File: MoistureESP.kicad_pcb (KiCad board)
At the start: 2 copper layers, 106 parts, among them J1 Conn_01x02_Pin, J2 Conn_MoisturePCB, J3 Conn_DS18B20, J4 Conn_01x06_Pin, J5 Conn_01x03_Pin, J7 USB4110-GF-A, Q1 SSM6K513NU-LF, Q10 SI7137DP-T1-GE3, Q2 SSM6K513NU-LF, Q3 2N7002W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

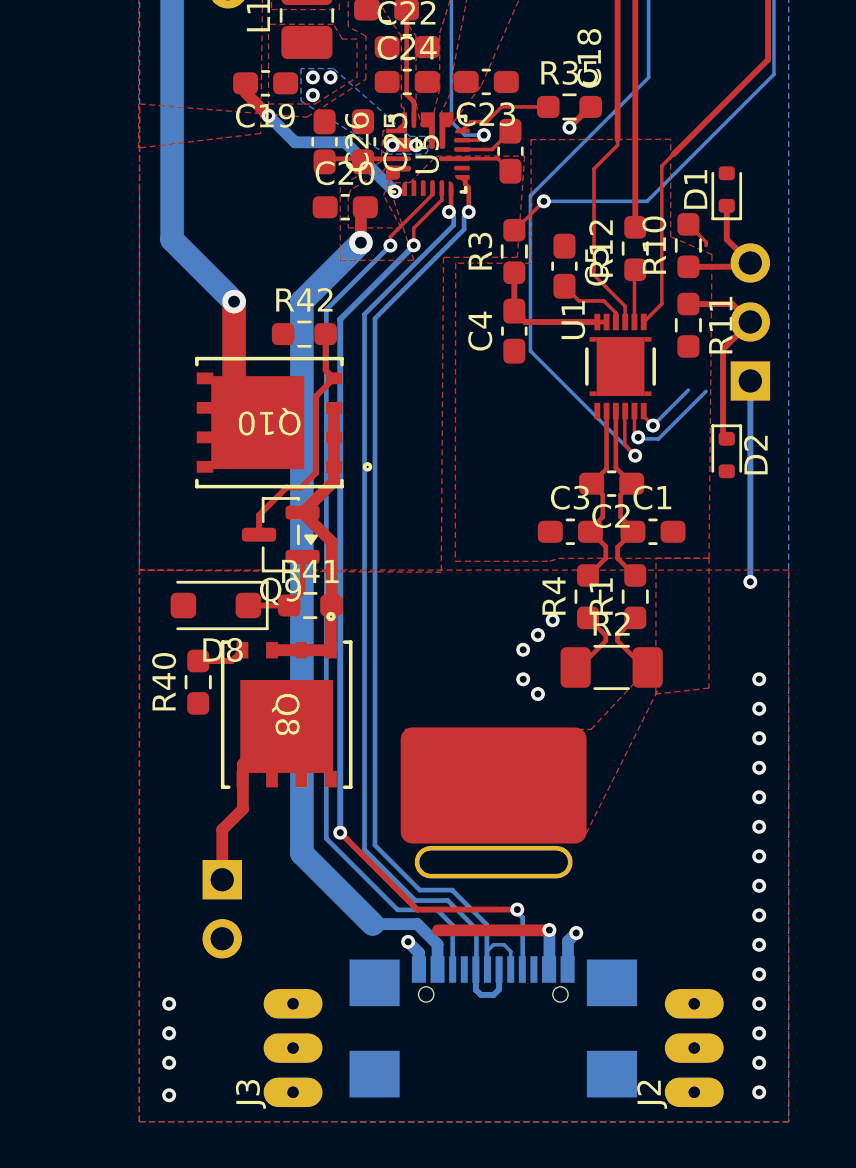
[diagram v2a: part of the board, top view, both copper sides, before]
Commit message: Change CGND connection to shunt resistor, change zone hierarchy.
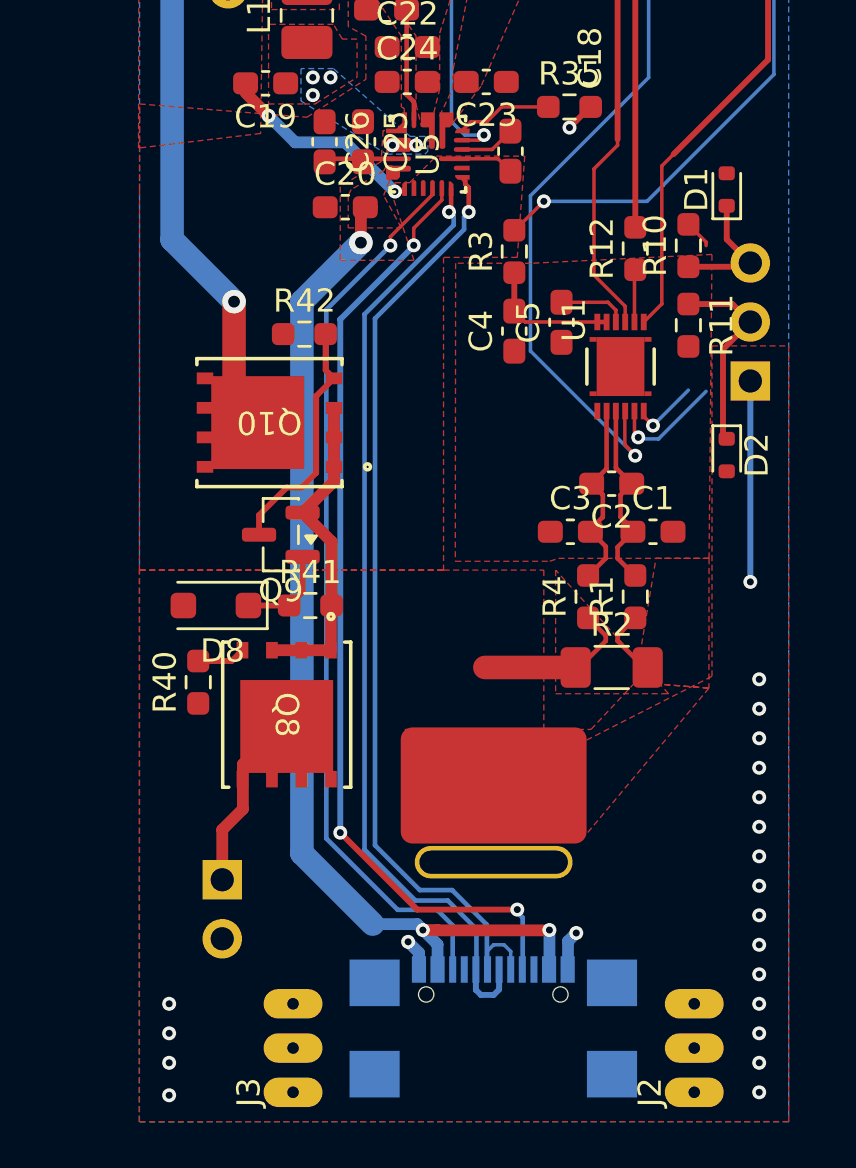
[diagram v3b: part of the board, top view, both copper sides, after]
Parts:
- moved C5 2.42 mm to (53.7, 118.0), turned to 90 degrees
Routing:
- net GNDPWR: track 15.7 -> 19.6 mm
- net VBUS: track 43.9 -> 44.6 mm, vias 2 -> 3
- net (no net): vias 24 -> 19
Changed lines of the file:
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@@
 	(footprint "Capacitor_SMD:C_0603_1608Metric_Pad1.08x0.95mm_HandSolder"
 		(layer "F.Cu")
-		(at 53.848 115.57 -90)
+		(at 53.721 117.983 90)
 		(descr "Capacitor SMD 0603 (1608 Metric), square (rectangular) end terminal, IPC-7351 nominal with elongated pad for handsoldering. (Body size source: IPC-SM-782 page 76, https://www.pcb-3d.com/wordpress/wp-content/uploads/ipc-sm-782a_amendment_1_and_2.pdf)")
 		(tags "capacitor handsolder")
@@
 		(duplicate_pad_numbers_are_jumpers no)
 		(fp_line
-			(start -0.146267 0.51)
-			(end 0.146267 0.51)
+			(start -0.146267 -0.51)
+			(end 0.146267 -0.51)
 			(stroke
 				(width 0.12)
@@
 		)
 		(fp_line
-			(start -0.146267 -0.51)
-			(end 0.146267 -0.51)
+			(start -0.146267 0.51)
+			(end 0.146267 0.51)
 			(stroke
 				(width 0.12)
@@
 		)
 		(pad "1" smd roundrect
-			(at -0.8625 0 270)
+			(at -0.8625 0 90)
 			(size 1.075 0.95)
 			(layers "F.Cu" "F.Mask" "F.Paste")
@@
 		)
 		(pad "2" smd roundrect
-			(at 0.8625 0 270)
+			(at 0.8625 0 90)
 			(size 1.075 0.95)
 			(layers "F.Cu" "F.Mask" "F.Paste")
@@
 	)
 	(via
-		(at 52.705 131.445)
-		(size 0.6)
-		(drill 0.3)
-		(layers "F.Cu" "B.Cu")
-		(net "")
-	)
-	(via
 		(at 62.23 143.51)
 		(size 0.6)
@@
 	)
 	(via
-		(at 53.34 130.81)
-		(size 0.6)
-		(drill 0.3)
-		(layers "F.Cu" "B.Cu")
-		(net "")
-	)
-	(via
-		(at 52.705 133.985)
-		(size 0.6)
-		(drill 0.3)
-		(layers "F.Cu" "B.Cu")
-		(net "")
-	)
-	(via
 		(at 36.83 148.59)
 		(size 0.6)
@@
 	)
 	(via
-		(at 52.07 132.08)
-		(size 0.6)
-		(drill 0.3)
-		(layers "F.Cu" "B.Cu")
-		(net "")
-	)
-	(via
 		(at 62.23 146.05)
 		(size 0.6)
@@
 	)
 	(via
-		(at 52.07 133.35)
-		(size 0.6)
-		(drill 0.3)
-		(layers "F.Cu" "B.Cu")
-		(net "")
-	)
-	(via
 		(at 62.23 148.59)
 		(size 0.6)
@@
 	)
 	(segment
+		(start 54.33 132.842)
+		(end 50.419 132.842)
+		(width 1.016)
+		(layer "F.Cu")
+		(net "GNDPWR")
+	)
+	(segment
 		(start 51.3435 107.636)
 		(end 51.3435 107.622)
@@
 	)
 	(segment
-		(start 54.4809 117.0654)
-		(end 53.848 116.4325)
-		(width 0.1524)
-		(layer "F.Cu")
-		(net "Net-(U1-PBI)")
-	)
-	(segment
-		(start 55.543501 117.0654)
-		(end 54.4809 117.0654)
+		(start 55.7192 117.1205)
+		(end 53.721 117.1205)
 		(width 0.1524)
 		(layer "F.Cu")
@@
 	(segment
 		(start 56.061 117.9703)
-		(end 56.061 117.582899)
+		(end 56.061 117.4623)
 		(width 0.1524)
 		(layer "F.Cu")
@@
 	)
 	(segment
-		(start 56.061 117.582899)
-		(end 55.543501 117.0654)
+		(start 56.061 117.4623)
+		(end 55.7192 117.1205)
 		(width 0.1524)
 		(layer "F.Cu")
@@
 	(segment
 		(start 52.1578 117.9703)
-		(end 51.689 117.5015)
-		(width 0.254)
+		(end 55.260999 117.9703)
+		(width 0.1524)
 		(layer "F.Cu")
 		(net "Net-(U1-VC1)")
@@
 	)
 	(segment
-		(start 55.661001 117.9703)
-		(end 55.661001 117.764001)
+		(start 51.689 117.5015)
+		(end 52.1578 117.9703)
 		(width 0.1524)
 		(layer "F.Cu")
@@
 	)
 	(segment
-		(start 55.260999 117.9703)
-		(end 52.1578 117.9703)
-		(width 0.254)
+		(start 55.661001 117.9703)
+		(end 55.661001 117.764001)
+		(width 0.1524)
 		(layer "F.Cu")
 		(net "Net-(U1-VC1)")
@@
 	)
 	(segment
+		(start 46.5105 110.144001)
+		(end 47.113501 110.144001)
+		(width 0.2)
+		(layer "F.Cu")
+		(net "Net-(U5-LX)")
+	)
+	(via
+		(at 43.0145 108.204)
+		(size 0.6)
+		(drill 0.3)
+		(layers "F.Cu" "B.Cu")
+		(free yes)
+		(net "Net-(U5-LX)")
+	)
+	(via
+		(at 43.7765 107.442)
+		(size 0.6)
+		(drill 0.3)
+		(layers "F.Cu" "B.Cu")
+		(free yes)
+		(net "Net-(U5-LX)")
+	)
+	(via
+		(at 46.4435 110.363)
+		(size 0.6)
+		(drill 0.3)
+		(layers "F.Cu" "B.Cu")
+		(net "Net-(U5-LX)")
+	)
+	(via
+		(at 43.0145 107.442)
+		(size 0.6)
+		(drill 0.3)
+		(layers "F.Cu" "B.Cu")
+		(free yes)
+		(net "Net-(U5-LX)")
+	)
+	(via
+		(at 47.4595 110.363)
+		(size 0.6)
+		(drill 0.3)
+		(layers "F.Cu" "B.Cu")
+		(net "Net-(U5-LX)")
+	)
+	(segment
 		(start 36.365999 92.0175)
 		(end 36.806 92.457501)
@@
 	(segment
 		(start 48.4 144.158)
+		(end 48.387 144.145)
+		(width 0.508)
+		(layer "F.Cu")
+		(net "VBUS")
+	)
+	(segment
+		(start 48.4 144.158)
 		(end 53.187 144.158)
 		(width 0.508)
@@
 	)
 	(segment
+		(start 48.387 144.145)
+		(end 47.752 144.145)
+		(width 0.508)
+		(layer "F.Cu")
+		(net "VBUS")
+	)
+	(segment
 		(start 45.085 114.554)
 		(end 45.085 113.219)
@@
 		(net "VBUS")
 	)
+	(via
+		(at 47.752 144.145)
+		(size 0.6)
+		(drill 0.3)
+		(layers "F.Cu" "B.Cu")
+		(net "VBUS")
+	)
 	(segment
 		(start 42.545 140.843)
@@
 		(net "Net-(U5-IFAST)")
 	)
-	(segment
-		(start 46.5105 110.144001)
-		(end 47.113501 110.144001)
-		(width 0.2)
-		(layer "F.Cu")
-		(net "Net-(U5-LX)")
-	)
-	(via
-		(at 43.0145 108.204)
-		(size 0.6)
-		(drill 0.3)
-		(layers "F.Cu" "B.Cu")
-		(free yes)
-		(net "Net-(U5-LX)")
-	)
-	(via
-		(at 43.7765 107.442)
-		(size 0.6)
-		(drill 0.3)
-		(layers "F.Cu" "B.Cu")
-		(free yes)
-		(net "Net-(U5-LX)")
-	)
-	(via
-		(at 46.4435 110.363)
-		(size 0.6)
-		(drill 0.3)
-		(layers "F.Cu" "B.Cu")
-		(net "Net-(U5-LX)")
-	)
-	(via
-		(at 43.0145 107.442)
-		(size 0.6)
-		(drill 0.3)
-		(layers "F.Cu" "B.Cu")
-		(free yes)
-		(net "Net-(U5-LX)")
-	)
-	(via
-		(at 47.4595 110.363)
-		(size 0.6)
-		(drill 0.3)
-		(layers "F.Cu" "B.Cu")
-		(net "Net-(U5-LX)")
-	)
 	(zone
 		(net "GNDPWR")
@@
 		(name "gndpwr")
 		(hatch edge 0.5)
-		(priority 9)
+		(priority 6)
 		(connect_pads
 			(clearance 0.254)
@@
 		(polygon
 			(pts
-				(xy 35.550764 128.652242) (xy 63.5 128.649758) (xy 63.5 152.4) (xy 35.548751 152.397632)
+				(xy 52.959 128.651) (xy 52.959 136.906) (xy 60.198 133.223) (xy 60.198 118.999) (xy 63.5 118.999)
+				(xy 63.5 143.002) (xy 63.502508 152.390163) (xy 35.548751 152.397632) (xy 35.550764 128.652242)
+				(xy 48.642663 128.650543)
+			)
+		)
+		(polygon
+			(pts
+				(xy 53.466702 128.651) (xy 53.467296 133.972268) (xy 58.293 133.971732) (xy 58.33 133.972)
 			)
 		)
@@
 		(net "CGND")
 		(layer "F.Cu")
-		(name "GNDCELL_POUR")
+		(name "CGND_BRIDGE_TO_BQ")
 		(hatch edge 0.5)
-		(priority 1)
+		(priority 12)
 		(connect_pads
-			(clearance 0.5)
+			(clearance 0.1524)
 		)
 		(min_thickness 0.25)
@@
 		(polygon
 			(pts
-				(xy 60.066709 133.732413) (xy 57.781886 133.985) (xy 57.788116 128.144) (xy 60.07099 128.144)
+				(xy 60.066709 133.732413) (xy 56.896 133.477) (xy 57.788116 128.144) (xy 60.07099 128.144)
 			)
 		)
@@
 		(name "Vbat")
 		(hatch edge 0.5)
-		(priority 3)
+		(priority 1)
 		(connect_pads yes
 			(clearance 0.1524)
@@
 		(name "VBATP")
 		(hatch edge 0.5)
-		(priority 12)
+		(priority 9)
 		(connect_pads
 			(clearance 0.1524)
@@
 		(name "fests")
 		(hatch edge 0.5)
-		(priority 7)
+		(priority 5)
 		(connect_pads yes
 			(clearance 0.1524)
@@
 		(name "GNDPWR")
 		(hatch edge 0.5)
-		(priority 2)
 		(connect_pads yes
 			(clearance 0.1524)
@@
 		(name "VCELLIN")
 		(hatch edge 0.5)
-		(priority 11)
+		(priority 8)
 		(connect_pads yes
 			(clearance 0.1524)
@@
 		(net "CGND")
 		(layer "F.Cu")
-		(name "CGNDPOLY")
+		(name "CGND_TO_RESISTOR")
 		(hatch edge 0.5)
-		(priority 8)
+		(priority 11)
 		(connect_pads yes
 			(clearance 0.1524)
@@
 		(polygon
 			(pts
-				(xy 46.99 135.509) (xy 54.991 135.509) (xy 56.896 133.477) (xy 58.039 133.477) (xy 54.737 140.081)
+				(xy 46.99 135.509) (xy 54.991 135.509) (xy 56.896 133.477) (xy 60.066709 133.732413) (xy 54.737 140.081)
 				(xy 46.99 140.081)
 			)
@@
 		(name "VBUS")
 		(hatch edge 0.5)
-		(priority 5)
+		(priority 3)
 		(connect_pads yes
 			(clearance 0.1524)
@@
 		(name "cell")
 		(hatch edge 0.5)
-		(priority 6)
+		(priority 4)
 		(connect_pads yes
 			(clearance 0.1524)
@@
 		(net "CGND")
 		(layer "F.Cu")
-		(name "GNDCELL_POUR")
+		(name "CGND_BQ")
 		(hatch edge 0.5)
+		(priority 13)
 		(connect_pads
 			(clearance 0.254)
@@
 		(polygon
 			(pts
-				(xy 52.419 115.443) (xy 49.161834 115.439742) (xy 49.149 128.27) (xy 53.213 128.27) (xy 53.593765 128.144)
-				(xy 60.07099 128.144) (xy 60.198 115.062) (xy 58.42 114.3) (xy 58.42 110.109) (xy 52.407663 110.121809)
+				(xy 49.161834 115.439742) (xy 49.149 128.27) (xy 53.213 128.27) (xy 53.593765 128.144) (xy 60.07099 128.144)
+				(xy 60.198 115.062) (xy 52.407663 115.443)
 			)
 		)
@@
 		(name "GNDPWR")
 		(hatch edge 0.5)
-		(priority 10)
+		(priority 7)
 		(connect_pads yes
 			(clearance 0.1524)
@@
 				(xy 45.957023 111.063636) (xy 44.196 112.141) (xy 44.196 115.313685) (xy 47.371 115.316) (xy 46.422471 112.481066)
 				(xy 46.549471 111.973066) (xy 47.184471 111.973066) (xy 48.327471 110.830066) (xy 52.137471 110.830066)
-				(xy 51.816 115.189) (xy 48.641 115.189) (xy 48.543206 128.745963) (xy 35.550764 128.652242) (xy 35.55586 112.268)
+				(xy 51.816 115.189) (xy 48.641 115.189) (xy 48.642705 128.650584) (xy 35.550764 128.652242) (xy 35.55586 112.268)
 				(xy 35.56 108.585) (xy 42.7605 109.156501) (xy 45.3005 107.523644) (xy 45.3005 105.664) (xy 44.5395 105.251)
 				(xy 44.5395 103.791) (xy 45.5545 103.759)
@@
 		(name "bst")
 		(hatch edge 0.5)
-		(priority 4)
+		(priority 2)
 		(connect_pads yes
 			(clearance 0.1524)
@@
 		(net "Net-(U5-LX)")
 		(layer "B.Cu")
-		(name "cbstnet")
+		(name "CBST_POLY")
 		(hatch edge 0.5)
 		(priority 14)
@@
 		(name "GNDCELL_POUR")
 		(hatch edge 0.5)
-		(priority 13)
+		(priority 10)
 		(connect_pads
 			(clearance 0.1524)

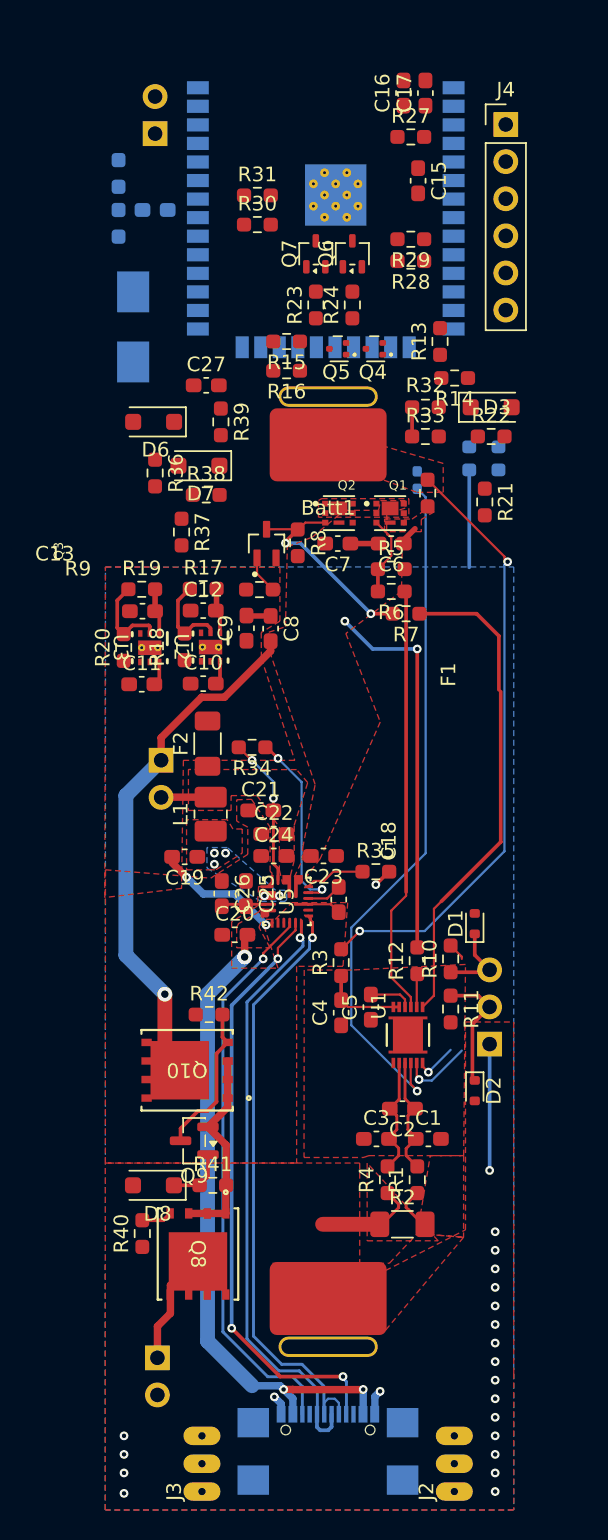
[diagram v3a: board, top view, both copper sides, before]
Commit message: Refine VBAT zone and add wiring under MCU.
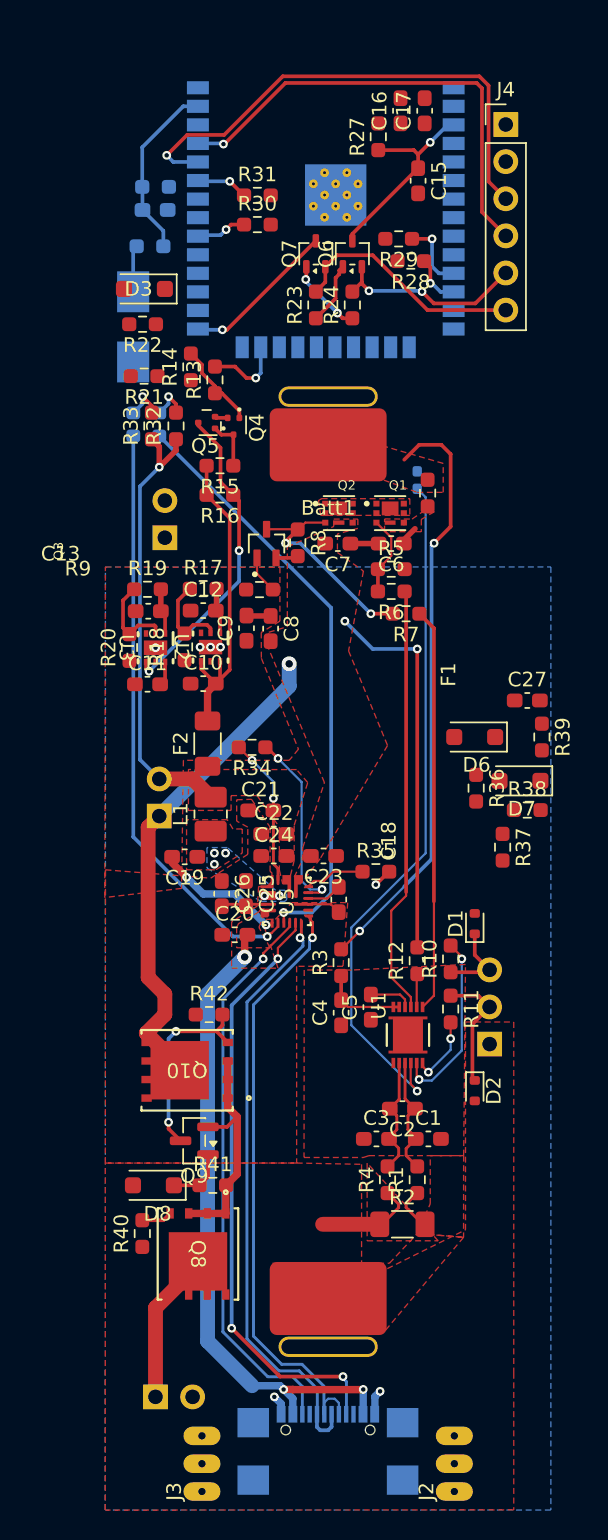
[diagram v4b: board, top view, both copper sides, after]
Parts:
- moved C27 30.8 mm to (64.4, 97.0)
- moved R38 30.8 mm to (64.4, 104.5)
- moved R39 30.8 mm to (65.4, 99.5)
- moved D6 30.8 mm to (60.8, 99.5)
- moved D7 30.8 mm to (63.9, 102.5)
- moved R36 30.8 mm to (60.9, 103.0)
- moved R37 30.8 mm to (62.7, 107.0)
- moved JP2 27.7 mm to (39.6, 85.9)
- moved D3 25.1 mm to (38.2, 68.8), turned to 180 degrees
- moved R22 25.1 mm to (38.1, 71.2), turned to 180 degrees
- moved R21 24.9 mm to (38.2, 74.8), turned to 180 degrees
- moved D4 23.3 mm to (39.2, 78.1)
- moved D5 23.1 mm to (37.5, 78.1)
- moved R33 18.7 mm to (38.7, 78.2), turned to 90 degrees
- moved R14 18.1 mm to (41.4, 74.2), turned to 90 degrees
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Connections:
- net Net-(U2-EN) renamed /power/Vsysf
- J4 pad 2: GNDPWR -> GNDD
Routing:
- net Net-(D4-K): track 0.00 -> 40.7 mm, vias 0 -> 1
- net /mcu/MCU.RX: track 0.00 -> 35.1 mm, vias 0 -> 1
- net /charger/~{INOK}: track 6.66 -> 40.9 mm, vias 0 -> 1
- net /mcu/MCU.TX: track 0.00 -> 32.1 mm, vias 0 -> 1
- net Vsys: track 5.40 -> 31.0 mm, vias 0 -> 1
- net Net-(Q5-D): track 0.00 -> 21.5 mm, vias 0 -> 2
- net /power/Vsysf: track 3.31 -> 24.0 mm
- net /mcu/MCU.DTR: track 0.00 -> 16.2 mm
- net Net-(Q6-C): track 0.00 -> 13.9 mm, vias 0 -> 1
- net /mcu/MCU.RTS: track 0.00 -> 13.3 mm, vias 0 -> 2
- net /mcu/~{force_wakeup_prot}: track 0.00 -> 12.3 mm
- net /mcu/BOOT: track 0.00 -> 10.6 mm, vias 0 -> 1
- net GNDPWR: track 19.6 -> 11.9 mm, vias 4 -> 7
- net Net-(U1-SCL): track 6.22 -> 12.5 mm, vias 1 -> 2
- net Net-(Q4-G): track 0.00 -> 6.06 mm
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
